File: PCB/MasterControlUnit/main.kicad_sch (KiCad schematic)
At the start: 4 parts, among them U1 STM32F407G-DISC1

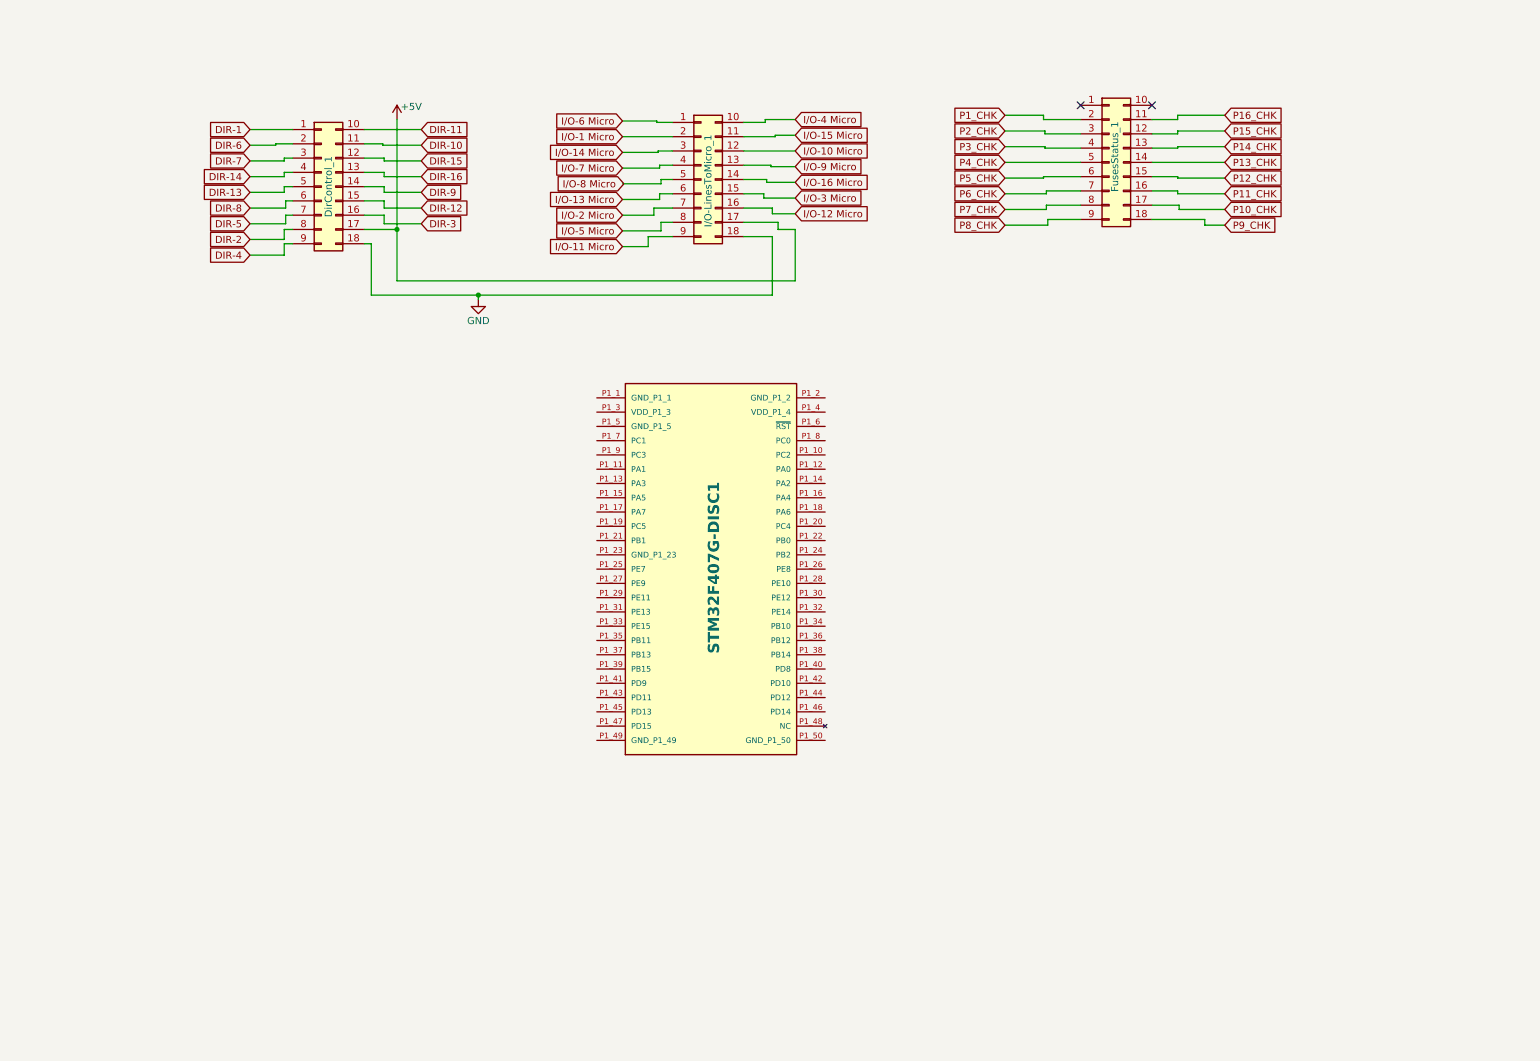
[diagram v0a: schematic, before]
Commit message: Under development
STM32's SPI and I2C buses have been connected
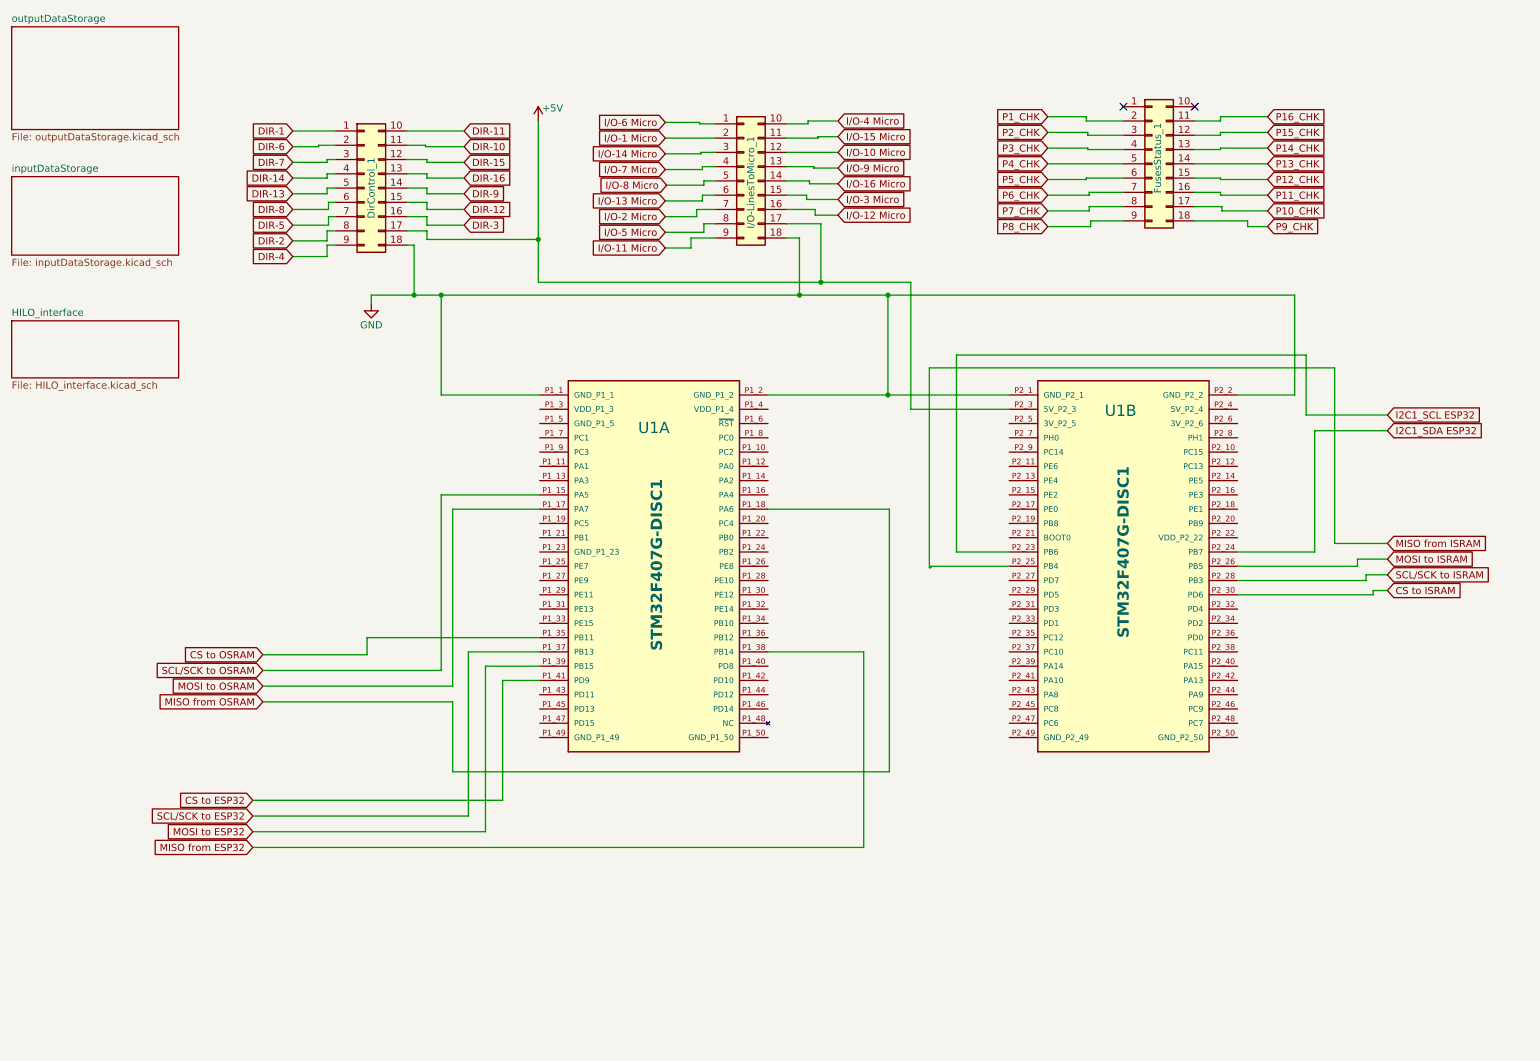
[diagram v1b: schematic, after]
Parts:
- added unit 2 of U1
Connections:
- net +5V: now also U1.P2_3 (5V_P2_3)
- net GND: now also U1.P1_1 (GND_P1_1), U1.P1_2 (GND_P1_2), U1.P2_1 (GND_P2_1), U1.P2_2 (GND_P2_2)
- net SCL/SCK to OSRAM: now reaches U1.P1_15 (PA5)
- net MOSI to OSRAM: now reaches U1.P1_17 (PA7)
- net MISO from OSRAM: now reaches U1.P1_18 (PA6)
- net CS to OSRAM: now reaches U1.P1_35 (PB11)
- net SCL/SCK to ESP32: now reaches U1.P1_37 (PB13)
- net MISO from ESP32: now reaches U1.P1_38 (PB14)
- net MOSI to ESP32: now reaches U1.P1_39 (PB15)
- net CS to ESP32: now reaches U1.P1_41 (PD9)
- new net CS to ISRAM: U1.P2_30 (PD6)
- new net I2C1_SCL ESP32: U1.P2_23 (PB6)
- new net I2C1_SDA ESP32: U1.P2_24 (PB7)
- new net MISO from ISRAM: U1.P2_25 (PB4)
- new net MOSI to ISRAM: U1.P2_26 (PB5)
- new net SCL/SCK to ISRAM: U1.P2_28 (PB3)
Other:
- added sheet HILO_interface (HILO_interface.kicad_sch)
- added sheet inputDataStorage (inputDataStorage.kicad_sch)
- added sheet outputDataStorage (outputDataStorage.kicad_sch)
- company: (none) -> Panicosoft
- title: (none) -> Master Control Unit (main)
- moved on the sheet: DirControl_1, FusesStatus_1, I/O-LinesToMicro_1

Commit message: Under development ver
inputDataStorage.kicad_sch will be renamed to dataStorages.kicad_sch
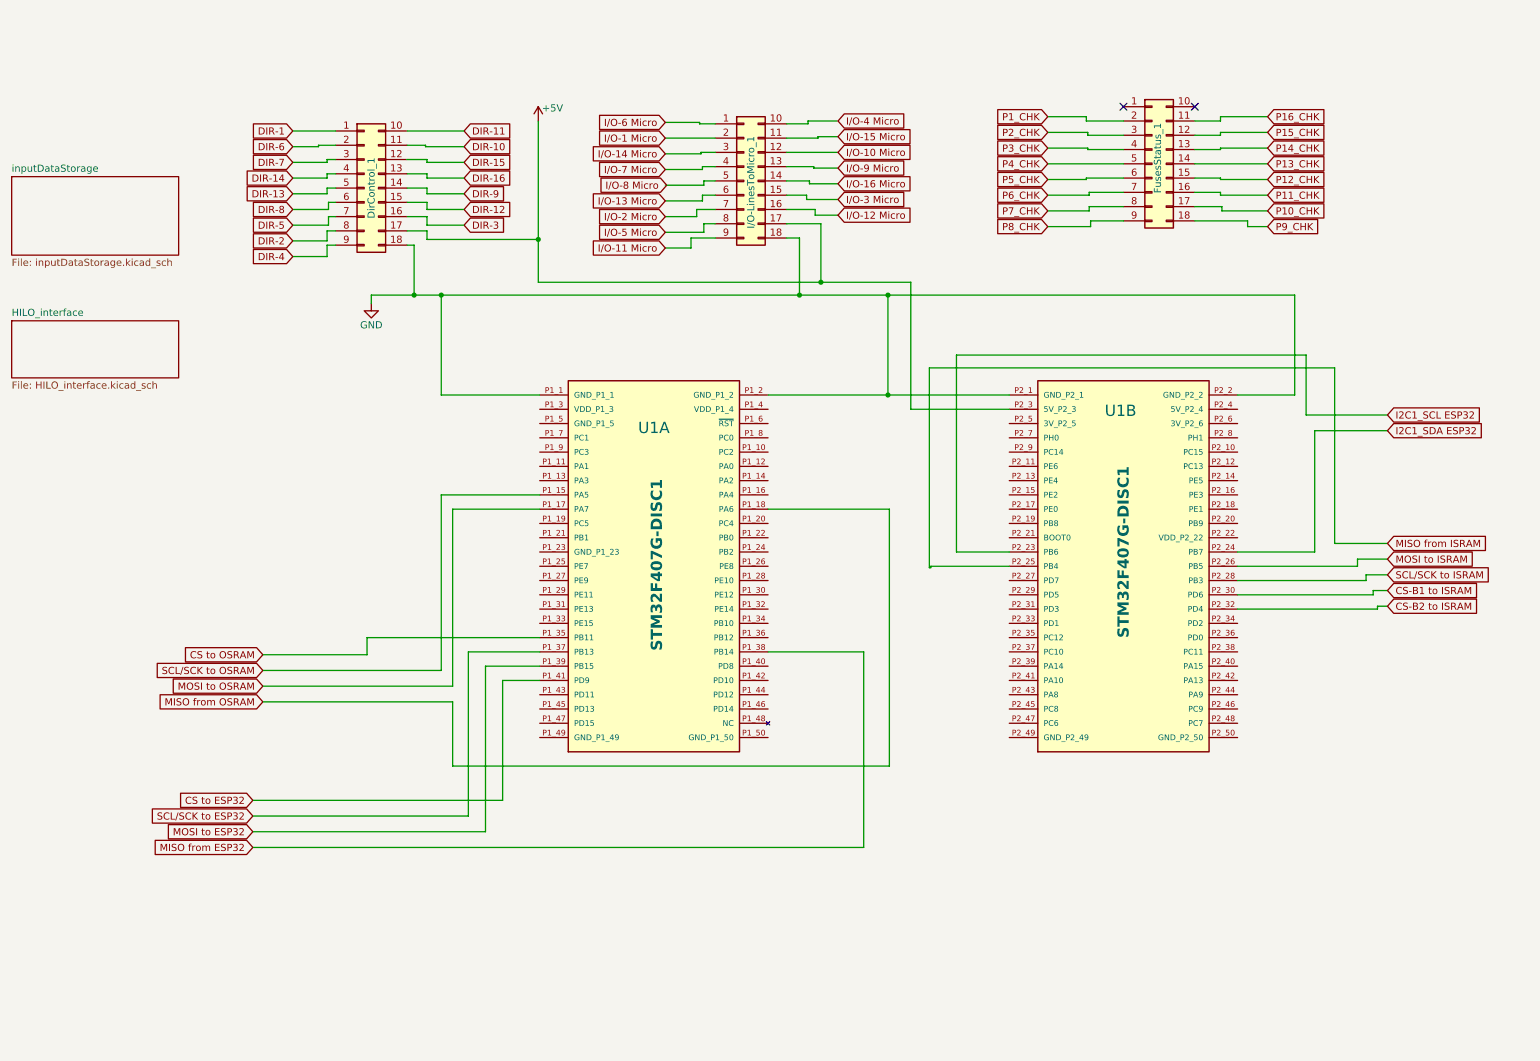
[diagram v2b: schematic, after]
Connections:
- net CS-B2 to ISRAM: now reaches U1.P2_32 (PD4)
- net CS to ISRAM renamed CS-B1 to ISRAM
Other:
- removed sheet outputDataStorage
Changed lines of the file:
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@@
 	(wire
 		(pts
+			(xy 234.95 119.634) (xy 259.842 119.634)
+		)
+		(stroke
+			(width 0)
+			(type default)
+		)
+	)
+	(wire
+		(pts
 			(xy 80.01 127.762) (xy 61.468 127.762)
 		)
@@
 	(wire
 		(pts
+			(xy 261.62 119.126) (xy 259.842 119.126)
+		)
+		(stroke
+			(width 0)
+			(type default)
+		)
+	)
+	(wire
+		(pts
 			(xy 201.168 43.18) (xy 208.026 43.18)
 		)
@@
 	(wire
 		(pts
+			(xy 259.842 119.126) (xy 259.842 119.634)
+		)
+		(stroke
+			(width 0)
+			(type default)
+		)
+	)
+	(wire
+		(pts
 			(xy 257.81 114.554) (xy 257.81 113.538)
 		)
@@
 	(wire
 		(pts
-			(xy 95.25 148.59) (xy 95.25 136.144)
+			(xy 95.25 147.574) (xy 95.25 136.144)
 		)
 		(stroke
@@
 	(wire
 		(pts
-			(xy 172.974 148.59) (xy 95.25 148.59)
+			(xy 172.974 147.574) (xy 95.25 147.574)
 		)
 		(stroke
@@
 	(wire
 		(pts
-			(xy 172.974 101.854) (xy 172.974 148.59)
+			(xy 172.974 101.854) (xy 172.974 147.574)
 		)
 		(stroke
@@
 		)
 	)
-	(global_label "CS to ISRAM"
+	(global_label "CS-B1 to ISRAM"
 		(shape input)
 		(at 261.62 116.332 0)
@@
 		)
 		(property "Intersheetrefs" "${INTERSHEET_REFS}"
-			(at 276.5189 116.332 0)
+			(at 280.5708 116.332 0)
 			(effects
 				(font
@@
 		)
 	)
+	(global_label "CS-B2 to ISRAM"
+		(shape input)
+		(at 261.62 119.126 0)
+		(fields_autoplaced yes)
+		(effects
+			(font
+				(size 1.27 1.27)
+			)
+			(justify left)
+		)
+		(property "Intersheetrefs" "${INTERSHEET_REFS}"
+			(at 280.5708 119.126 0)
+			(effects
+				(font
+					(size 1.27 1.27)
+				)
+				(justify left)
+				(hide yes)
+			)
+		)
+	)
 	(global_label "I{slash}O-7 Micro"
 		(shape input)
@@
 				)
 			)
-		)
-	)
-	(sheet
-		(at 16.764 16.002)
-		(size 29.718 18.288)
-		(exclude_from_sim no)
-		(in_bom yes)
-		(on_board yes)
-		(dnp no)
-		(fields_autoplaced yes)
-		(stroke
-			(width 0.1524)
-			(type solid)
-		)
-		(fill
-			(color 0 0 0 0.0000)
-		)
-		(property "Sheetname" "outputDataStorage"
-			(at 16.764 15.2904 0)
-			(effects
-				(font
-					(size 1.27 1.27)
-				)
-				(justify left bottom)
-			)
-		)
-		(property "Sheetfile" "outputDataStorage.kicad_sch"
-			(at 16.764 34.8746 0)
-			(effects
-				(font
-					(size 1.27 1.27)
-				)
-				(justify left top)
-			)
-		)
-		(instances
-			(project "main"
-				(path "/f4f7b7d6-300b-4628-9b40-5d3a43871a01"
-					(page "2")
-				)
-			)

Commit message: HILO's engine component is completed
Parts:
- added U15: MCP23017_SO, Package_SO:SOIC-28W_7.5x17.9mm_P1.27mm, symbol Interface_Expansion:MCP23017_SO
- added U5: LD1117S33TR_SOT223, Package_TO_SOT_SMD:SOT-223-3_TabPin2, symbol Regulator_Linear:LD1117S33TR_SOT223
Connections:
- net CS-B2 to ISRAM is gone; now on net OSRAM B-EN: U1.P2_32 (PD4)
- net +5V: now also U5.2 (VO)
- net DIR-1: now also U15.1 (GPB0)
- net DIR-10: now also U15.22 (GPA1)
- net DIR-11: now also U15.23 (GPA2)
- net DIR-12: now also U15.24 (GPA3)
- net DIR-13: now also U15.25 (GPA4)
- net DIR-14: now also U15.26 (GPA5)
- net DIR-15: now also U15.27 (GPA6)
- net DIR-16: now also U15.28 (GPA7)
- net DIR-2: now also U15.2 (GPB1)
- net DIR-3: now also U15.3 (GPB2)
- net DIR-4: now also U15.4 (GPB3)
- net DIR-5: now also U15.5 (GPB4)
- net DIR-6: now also U15.6 (GPB5)
- net DIR-7: now also U15.7 (GPB6)
- net DIR-8: now also U15.8 (GPB7)
- net DIR-9: now also U15.21 (GPA0)
- net GND: now also U15.10 (VSS), U5.1 (GND)
- net I2C1_SCL ESP32: now also U15.12 (SCK)
- net I2C1_SDA ESP32: now also U15.13 (SDA)
- net I/O-1 Micro: now also U1.P1_10 (PC2)
- net I/O-10 Micro: now also U1.P1_45 (PD13)
- net I/O-11 Micro: now also U1.P1_47 (PD15)
- net I/O-12 Micro: now also U1.P1_50 (GND_P1_50)
- net I/O-13 Micro: now also U1.P1_12 (PA0)
- net I/O-14 Micro: now also U1.P1_14 (PA2)
- net I/O-15 Micro: now also U1.P1_16 (PA4)
- net I/O-16 Micro: now also U1.P1_20 (PC4)
- net I/O-2 Micro: now also U1.P1_9 (PC3)
- net I/O-3 Micro: now also U1.P1_11 (PA1)
- net I/O-4 Micro: now also U1.P1_13 (PA3)
- net I/O-5 Micro: now also U1.P1_19 (PC5)
- net I/O-6 Micro: now also U1.P1_21 (PB1)
- net I/O-7 Micro: now also U1.P1_25 (PE7)
- net I/O-8 Micro: now also U1.P1_27 (PE9)
- net I/O-9 Micro: now also U1.P1_43 (PD11)
- net P10_CHK: now also U1.P2_22 (VDD_P2_22)
- net P11_CHK: now also U1.P2_34 (PD2)
- net P12_CHK: now also U1.P2_36 (PD0)
- net P13_CHK: now also U1.P2_38 (PC11)
- net P14_CHK: now also U1.P2_40 (PA15)
- net P15_CHK: now also U1.P2_42 (PA13)
- net P16_CHK: now also U1.P2_44 (PA9)
- net P1_CHK: now also U1.P2_4 (5V_P2_4)
- net P2_CHK: now also U1.P2_6 (3V_P2_6)
- net P3_CHK: now also U1.P2_46 (PC9)
- net P4_CHK: now also U1.P2_10 (PC15)
- net P5_CHK: now also U1.P2_12 (PC13)
- net P6_CHK: now also U1.P2_14 (PE5)
- net P7_CHK: now also U1.P2_16 (PE3)
- net P8_CHK: now also U1.P2_18 (PE1)
- net P9_CHK: now also U1.P2_48 (PC7)
- net PWM_2: now reaches U1.P2_20 (PB9)
- net PWM_1: now reaches U1.P2_45 (PC8)
- net OSRAM B-EN: now reaches U1.P1_29 (PE11)
- net OSRAM ADDR 2: now reaches U1.P1_31 (PE13)
- net OSRAM ADDR 1: now reaches U1.P1_33 (PE15)
- net at U1.P1_42 (PD10): now also U15.15 (A0)
- net at U1.P1_44 (PD12): now also U15.16 (A1)
- net at U1.P1_46 (PD14): now also U15.17 (A2)
- net STM32_reset: now reaches U1.P1_6 (~{RST})
- net STM32_reset: now also U15.18 (~{RESET})
- net ADC_2: now reaches U1.P1_7 (PC1)
- net ADC_1: now reaches U1.P1_8 (PC0)
- net CS to OSRAM renamed OSRAM ADDR 0
- net CS-B1 to ISRAM renamed ISRAM ADDR 0
- new net +3.3V: U15.9 (VDD), U5.3 (VI)
- no-connect marks 2 -> 15
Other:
- removed sheet HILO_interface
- sheet inputDataStorage: file inputDataStorage.kicad_sch -> testDataStorage.kicad_sch
- title: Master Control Unit (main) -> HILO's engine
- moved on the sheet: U1A

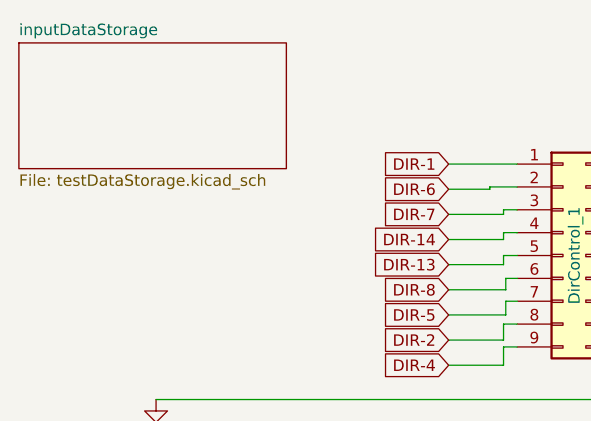
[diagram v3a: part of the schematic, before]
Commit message: Backup version
before to remove the SPI dedicated to the interative mode communication. In these modality the SPI is used by the STM32 to send
data stream the ESP32. Unfortunately the ESP32 can use just two SPI external ports
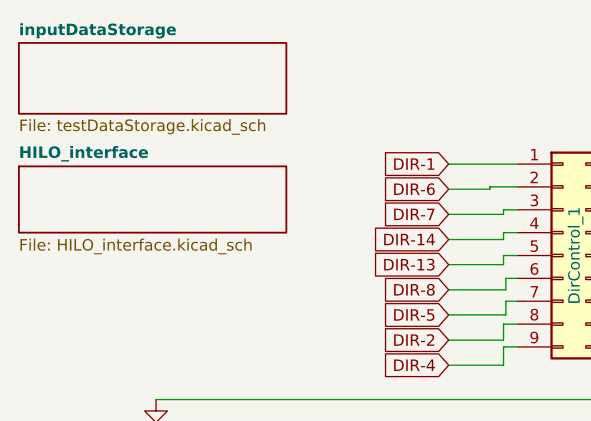
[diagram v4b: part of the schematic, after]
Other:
- added sheet HILO_interface (HILO_interface.kicad_sch)
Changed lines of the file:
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@@
 	(sheet
 		(at 19.05 21.082)
-		(size 29.718 13.97)
+		(size 29.718 7.874)
 		(exclude_from_sim no)
 		(in_bom yes)
@@
 		(fields_autoplaced yes)
 		(stroke
-			(width 0.1524)
+			(width 0.2)
 			(type solid)
 		)
@@
 				(font
 					(size 1.27 1.27)
+					(thickness 0.254)
+					(bold yes)
 				)
 				(justify left bottom)
@@
 		)
 		(property "Sheetfile" "testDataStorage.kicad_sch"
-			(at 19.05 35.6366 0)
+			(at 19.05 29.5406 0)
 			(effects
 				(font
+					(size 1.27 1.27)
+				)
+				(justify left top)
+			)
+		)
+		(instances
+			(project "main"
+				(path "/f4f7b7d6-300b-4628-9b40-5d3a43871a01"
+					(page "3")
+				)
+			)
+		)
+	)
+	(sheet
+		(at 19.05 34.798)
+		(size 29.718 7.366)
+		(exclude_from_sim no)
+		(in_bom yes)
+		(on_board yes)
+		(dnp no)
+		(fields_autoplaced yes)
+		(stroke
+			(width 0.2)
+			(type solid)
+		)
+		(fill
+			(color 0 0 0 0.0000)
+		)
+		(property "Sheetname" "HILO_interface"
+			(at 19.05 34.0126 0)
+			(effects
+				(font
+					(size 1.27 1.27)
+					(thickness 0.254)
+					(bold yes)
+				)
+				(justify left bottom)
+			)
+		)
+		(property "Sheetfile" "HILO_interface.kicad_sch"
+			(at 19.05 42.8224 0)
+			(effects
+				(font

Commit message: Important achitectural change (or fix)
Because ESP32 provides just two SPI ports, the original idea to use a dedicated SPI from STM32 to ESP32 cannot be implemented.
That SPI port was meant to be used in the interactive mode to send data from the STM32 to the ESP32.
The new idea is to use the SPI bus used to read/write the 64MB SRAM. The two MCU already shared that bus
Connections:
- net CS to ESP32 renamed CS
- net MISO from ESP32 renamed MISO
- net MOSI to ESP32 renamed MOSI
- net SCL/SCK to ESP32 renamed SCL/SCK
- net STM32_reset renamed MCU_reset
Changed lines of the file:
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@@
 	(wire
 		(pts
-			(xy 188.468 149.098) (xy 188.468 137.414)
+			(xy 188.468 146.812) (xy 188.468 137.414)
 		)
 		(stroke
@@
 	(wire
 		(pts
-			(xy 74.422 156.718) (xy 74.422 170.434)
+			(xy 74.422 137.414) (xy 74.422 170.434)
 		)
 		(stroke
@@
 	(wire
 		(pts
-			(xy 240.792 144.018) (xy 240.792 149.098)
+			(xy 240.792 144.018) (xy 240.792 146.812)
 		)
 		(stroke
@@
 	(wire
 		(pts
-			(xy 240.792 149.098) (xy 188.468 149.098)
+			(xy 240.792 146.812) (xy 188.468 146.812)
 		)
 		(stroke
@@
 	(wire
 		(pts
-			(xy 74.422 156.718) (xy 78.994 156.718)
+			(xy 74.422 137.414) (xy 78.994 137.414)
 		)
 		(stroke
@@
 	(wire
 		(pts
-			(xy 78.994 156.718) (xy 78.994 134.112)
+			(xy 78.994 137.414) (xy 78.994 134.112)
 		)
 		(stroke
@@
 		)
 	)
-	(global_label "MOSI to ESP32"
+	(global_label "MOSI"
 		(shape input)
 		(at 68.834 170.434 270)
@@
 		)
 		(property "Intersheetrefs" "${INTERSHEET_REFS}"
-			(at 68.834 187.8728 90)
+			(at 68.834 178.0154 90)
 			(effects
 				(font
@@
 		)
 	)
-	(global_label "SCL{slash}SCK to ESP32"
+	(global_label "SCL{slash}SCK"
 		(shape input)
 		(at 66.04 170.18 270)
@@
 		)
 		(property "Intersheetrefs" "${INTERSHEET_REFS}"
-			(at 66.04 191.6102 90)
+			(at 66.04 181.7528 90)
 			(effects
 				(font
@@
 		)
 	)
-	(global_label "STM32_reset"
+	(global_label "MCU_reset"
 		(shape input)
 		(at 153.67 178.816 270)
@@
 		)
 		(property "Intersheetrefs" "${INTERSHEET_REFS}"
-			(at 153.67 193.5335 90)
+			(at 153.67 191.5379 90)
 			(effects
 				(font
@@
 		)
 	)
-	(global_label "MISO from ESP32"
+	(global_label "MISO"
 		(shape input)
 		(at 74.422 170.434 270)
@@
 		)
 		(property "Intersheetrefs" "${INTERSHEET_REFS}"
-			(at 74.422 190.3523 90)
+			(at 74.422 178.0154 90)
 			(effects
 				(font
@@
 		)
 	)
-	(global_label "CS to ESP32"
+	(global_label "CS"
 		(shape input)
 		(at 71.628 170.434 270)
@@
 		)
 		(property "Intersheetrefs" "${INTERSHEET_REFS}"
-			(at 71.628 185.7561 90)
+			(at 71.628 175.8987 90)
 			(effects
 				(font
